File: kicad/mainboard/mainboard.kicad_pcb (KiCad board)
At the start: 2 copper layers, 40 x 64 mm, 37 parts, among them J1 USB_C_Receptacle_USB2.0_16P, J2 Conn_01x07_Socket, J3 Conn_01x06_Socket, J4 Conn_01x03_Socket, J5 Conn_01x07_Socket, SW1 FSM2JSMAATR, SW2 FSM2JSMAATR, U1 TPD1E05U06DYA, U2 TPD1E05U06DYA, U3 ESP32-S3-WROOM-1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

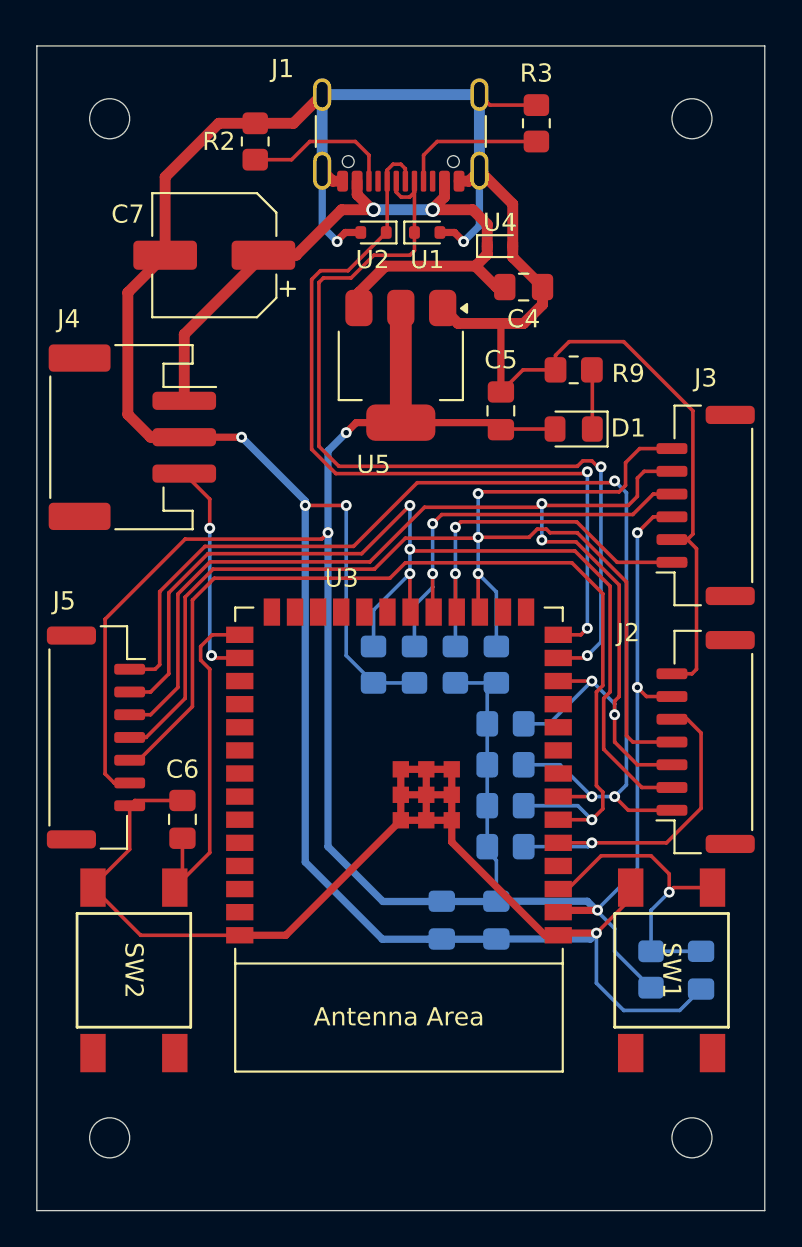
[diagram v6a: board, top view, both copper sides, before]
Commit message: remove buttons
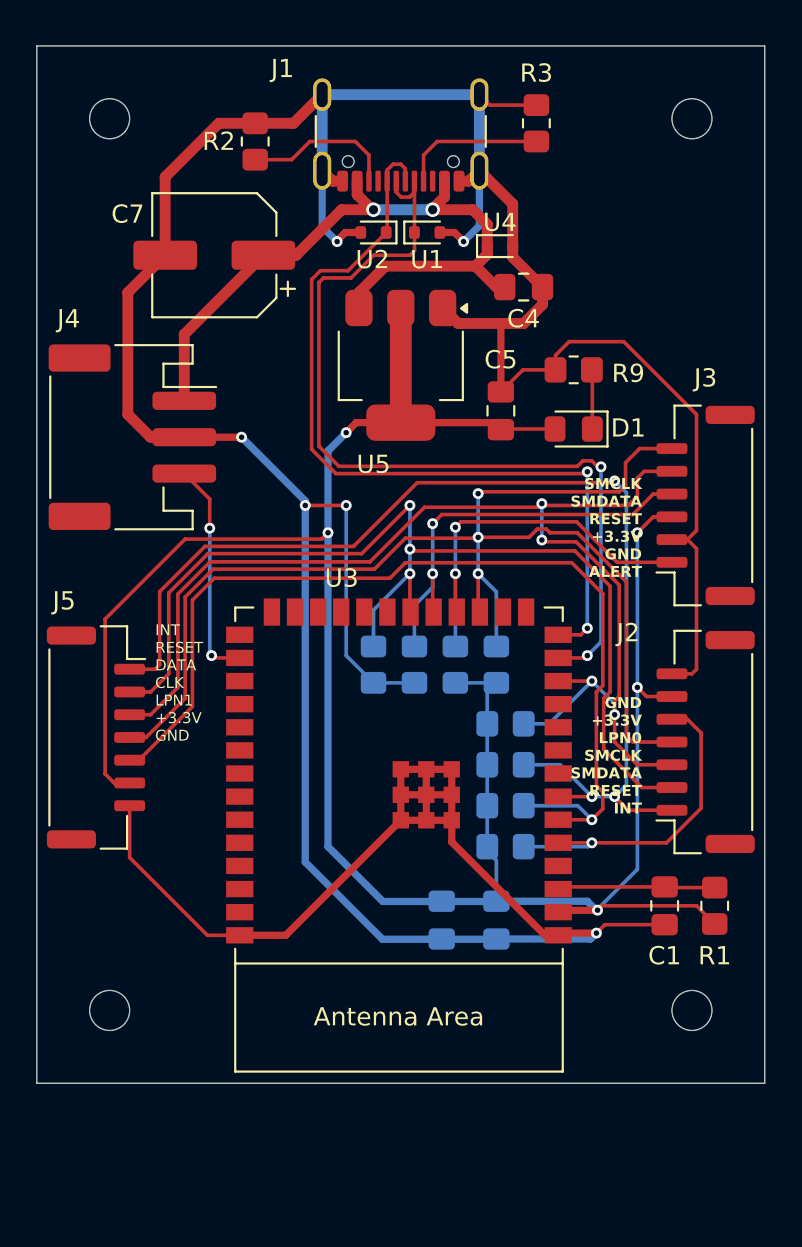
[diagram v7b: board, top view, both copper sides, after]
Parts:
- removed C6: 0.1uF, Capacitor_SMD:C_0805_2012Metric_Pad1.18x1.45mm_HandSolder
- removed SW1, SW2: FSM2JSMAATR, FSM2JSMAATR:SWITCH_FSM2JSMAA_TYC
- C1, R1: moved to F.Cu
- moved H3 7.00 mm to (108.2, 117.2)
- moved H4 7.00 mm to (140.2, 117.2)
- moved R1 4.95 mm to (141.5, 111.5)
- moved C1 4.06 mm to (138.8, 111.5)
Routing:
- net GPIO0: track 19.6 -> 0.00 mm
- net GND: track 242.8 -> 227.1 mm
- net EN: track 17.2 -> 8.66 mm, vias 1 -> 0
- net +3.3V: track 130.2 -> 131.6 mm
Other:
- board size 40 x 64 mm -> 40 x 57 mm
- board text added: "GND +3.3V LPN0 SMCLK SMDATA RESET INT"
- board text added: "INT RESET DATA CLK LPN1 +3.3V GND"
- board text added: "SMCLK SMDATA RESET +3.3V GND ALERT"

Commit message: remove switches
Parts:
- removed C7: 100uF, Capacitor_SMD:CP_Elec_6.3x5.8
- added C6: 100uF, Capacitor_SMD:CP_Elec_6.3x5.8, F.Cu at (114.0, 75.8)
- moved G*** 0.56 mm to (138.5, 75.0)
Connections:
- net EN renamed Net-(U3-EN)
- U3 pad 27: GPIO0 -> unconnected-(U3-GPIO0/BOOT-Pad27)
